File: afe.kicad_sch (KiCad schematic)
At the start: 142 parts, among them J1 Conn_01x18, Q1 Q_NMOS_GDS, Q10 Q_NMOS_GDS, Q11 Q_NMOS_GDS, Q12 Q_NMOS_GDS, Q13 Q_NMOS_GDS, Q14 Q_NMOS_GDS, Q15 Q_NMOS_GDS, Q16 Q_NMOS_GDS, Q17 Q_NMOS_GDS, Q18 Q_NMOS_GDS, Q19 Q_NMOS_GDS, Q2 Q_NMOS_GDS, Q20 Q_NMOS_GDS, Q21 Q_NMOS_GDS, Q22 Q_NMOS_GDS, Q23 Q_NMOS_GDS, Q24 Q_NMOS_GDS, Q25 Q_NMOS_GDS, Q26 Q_NMOS_GDS, Q3 Q_PMOS_GDS, Q4 Q_NPN_BCE, U1 PB7170P48

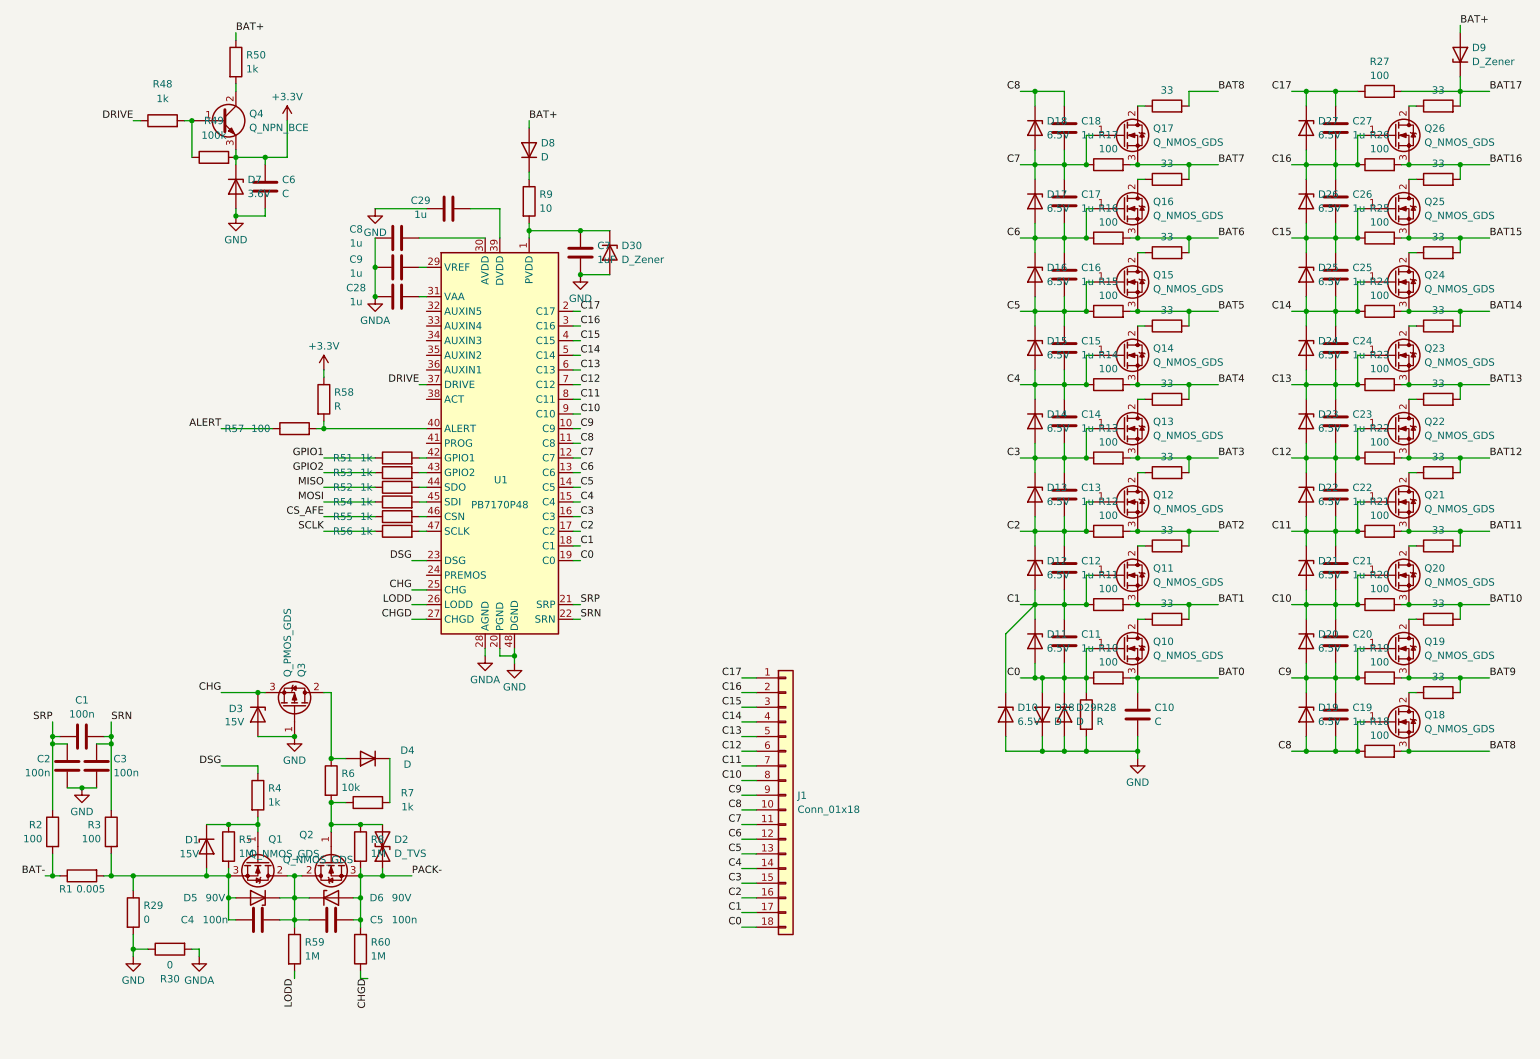
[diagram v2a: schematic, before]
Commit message: AFE改为PB7170(LQFP-64)，修改原理图，调整元器件布局
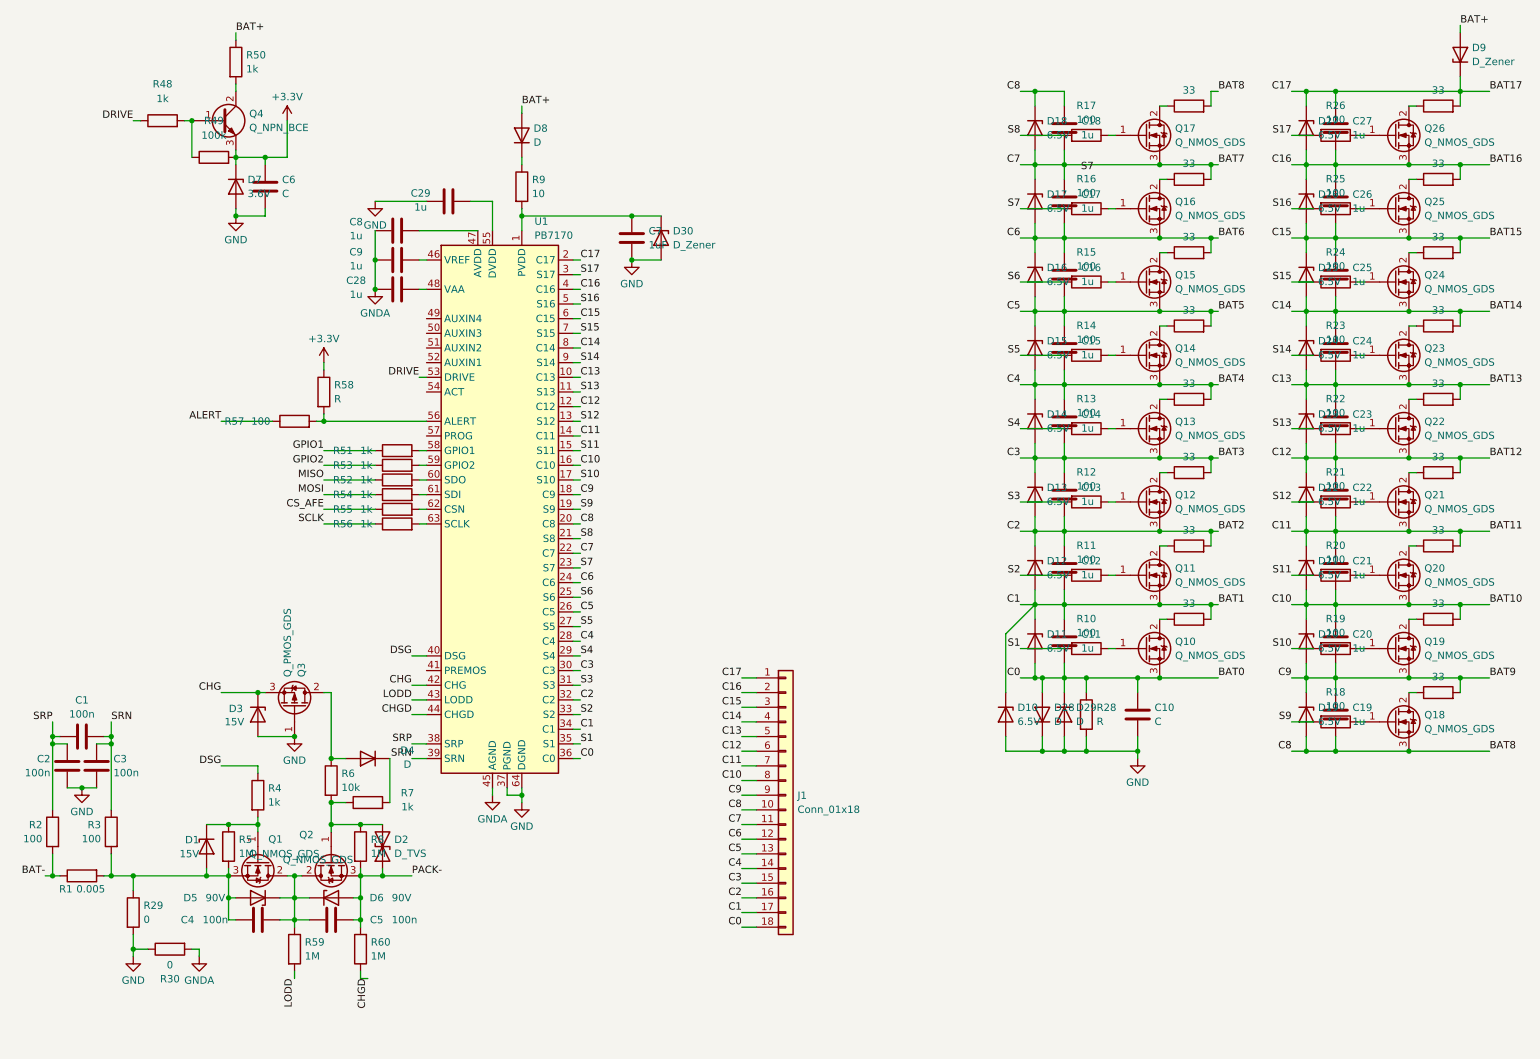
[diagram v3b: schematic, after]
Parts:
- removed R27: 100, Resistor_SMD:R_0603_1608Metric, symbol Device:R
- removed U1: PB7170P48, Package_QFP:LQFP-48_7x7mm_P0.5mm, symbol project_symbols:PB7170P48
- added U1: PB7170, Package_QFP:LQFP-64_10x10mm_P0.5mm, symbol project_symbols:PB7170
- C28, C29, C8, C9: footprint Capacitor_SMD:C_0603_1608Metric -> Capacitor_SMD:C_0402_1005Metric
- R10, R11, R12, R13, R14, R15, R16, R17, R18, R19, R2, R20, R21, R22, R23, R24, R25, R26, R3: footprint Resistor_SMD:R_0603_1608Metric -> Resistor_SMD:R_0402_1005Metric
- R31, R32, R33, R34, R35, R36, R37, R38, R39, R40, R41, R42, R43, R44, R45, R46, R47: footprint Resistor_SMD:R_0603_1608Metric -> Resistor_SMD:R_1206_3216Metric
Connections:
- net C17 is gone; now on net BAT17: C27.1, D27.1 (K), J1.1 (Pin_1)
- net BAT0: now also C11.2, D11.2 (A), D28.2 (A), D29.1 (K), J1.18 (Pin_18), R28.1, U1.36 (C0); no longer R10.2
- net BAT1: now also C11.1, C12.2, D10.1 (K), D11.1 (K), D12.2 (A), J1.17 (Pin_17), U1.34 (C1); no longer R11.2
- net BAT10: now also C20.1, C21.2, D20.1 (K), D21.2 (A), J1.8 (Pin_8), U1.16 (C10); no longer R20.2
- net BAT11: now also C21.1, C22.2, D21.1 (K), D22.2 (A), J1.7 (Pin_7), U1.14 (C11); no longer R21.2
- net BAT12: now also C22.1, C23.2, D22.1 (K), D23.2 (A), J1.6 (Pin_6), U1.12 (C12); no longer R22.2
- net BAT13: now also C23.1, C24.2, D23.1 (K), D24.2 (A), J1.5 (Pin_5), U1.10 (C13); no longer R23.2
- net BAT14: now also C24.1, C25.2, D24.1 (K), D25.2 (A), J1.4 (Pin_4), U1.8 (C14); no longer R24.2
- net BAT15: now also C25.1, C26.2, D25.1 (K), D26.2 (A), J1.3 (Pin_3), U1.6 (C15); no longer R25.2
- net BAT16: now also C26.1, C27.2, D26.1 (K), D27.2 (A), J1.2 (Pin_2), U1.4 (C16); no longer R26.2
- net BAT17: now also U1.2 (C17)
- net BAT2: now also C12.1, C13.2, D12.1 (K), D13.2 (A), J1.16 (Pin_16), U1.32 (C2); no longer R12.2
- net BAT3: now also C13.1, C14.2, D13.1 (K), D14.2 (A), J1.15 (Pin_15), U1.30 (C3); no longer R13.2
- net BAT4: now also C14.1, C15.2, D14.1 (K), D15.2 (A), J1.14 (Pin_14), U1.28 (C4); no longer R14.2
- net BAT5: now also C15.1, C16.2, D15.1 (K), D16.2 (A), J1.13 (Pin_13), U1.26 (C5); no longer R15.2
- net BAT6: now also C16.1, C17.2, D16.1 (K), D17.2 (A), J1.12 (Pin_12), U1.24 (C6); no longer R16.2
- net BAT7: now also C17.1, C18.2, D17.1 (K), D18.2 (A), J1.11 (Pin_11), U1.22 (C7); no longer R17.2
- net BAT8: now also C18.1, C19.2, D18.1 (K), D19.2 (A), J1.10 (Pin_10), U1.20 (C8); no longer R18.2
- net BAT9: now also C19.1, C20.2, D19.1 (K), D20.2 (A), J1.9 (Pin_9), U1.18 (C9); no longer R19.2
- net CHG: now also U1.42 (CHG)
- net CHGD: now also U1.44 (CHGD)
- net DRIVE: now also U1.53 (DRIVE)
- net DSG: now also U1.40 (DSG)
- net GND: now also U1.37 (PGND), U1.64 (DGND)
- net GNDA: now also U1.45 (AGND)
- net LODD: now also U1.43 (LODD)
- net SRN: now also U1.39 (SRN)
- net SRP: now also U1.38 (SRP)
- net at R54.2: now also U1.61 (SDI)
- net at C7.1, D30.1 (K), R9.2: now also U1.1 (PVDD)
- net at R53.2: now also U1.59 (GPIO2)
- net at C28.2: now also U1.48 (VAA)
- net at R52.2: now also U1.60 (SDO)
- net at C29.2: now also U1.55 (DVDD)
- net at R56.2: now also U1.63 (SCLK)
- net at C9.2: now also U1.46 (VREF)
- net at C8.2: now also U1.47 (AVDD)
- net at R57.2, R58.2: now also U1.56 (ALERT)
- net at R51.2: now also U1.58 (GPIO1)
- net at R55.2: now also U1.62 (CSN)
- removed net C0: C11.2, D11.2 (A), D28.2 (A), D29.1 (K), J1.18 (Pin_18), Q10.1 (G), R10.1, R28.1
- removed net C1: C11.1, C12.2, D10.1 (K), D11.1 (K), D12.2 (A), J1.17 (Pin_17), Q11.1 (G), R11.1
- removed net C10: C20.1, C21.2, D20.1 (K), D21.2 (A), J1.8 (Pin_8), Q20.1 (G), R20.1
- removed net C11: C21.1, C22.2, D21.1 (K), D22.2 (A), J1.7 (Pin_7), Q21.1 (G), R21.1
- removed net C12: C22.1, C23.2, D22.1 (K), D23.2 (A), J1.6 (Pin_6), Q22.1 (G), R22.1
- removed net C13: C23.1, C24.2, D23.1 (K), D24.2 (A), J1.5 (Pin_5), Q23.1 (G), R23.1
- removed net C14: C24.1, C25.2, D24.1 (K), D25.2 (A), J1.4 (Pin_4), Q24.1 (G), R24.1
- removed net C15: C25.1, C26.2, D25.1 (K), D26.2 (A), J1.3 (Pin_3), Q25.1 (G), R25.1
- removed net C16: C26.1, C27.2, D26.1 (K), D27.2 (A), J1.2 (Pin_2), Q26.1 (G), R26.1
- removed net C2: C12.1, C13.2, D12.1 (K), D13.2 (A), J1.16 (Pin_16), Q12.1 (G), R12.1
- removed net C3: C13.1, C14.2, D13.1 (K), D14.2 (A), J1.15 (Pin_15), Q13.1 (G), R13.1
- removed net C4: C14.1, C15.2, D14.1 (K), D15.2 (A), J1.14 (Pin_14), Q14.1 (G), R14.1
- removed net C5: C15.1, C16.2, D15.1 (K), D16.2 (A), J1.13 (Pin_13), Q15.1 (G), R15.1
- removed net C6: C16.1, C17.2, D16.1 (K), D17.2 (A), J1.12 (Pin_12), Q16.1 (G), R16.1
- removed net C7: C17.1, C18.2, D17.1 (K), D18.2 (A), J1.11 (Pin_11), Q17.1 (G), R17.1
- removed net C8: C18.1, C19.2, D18.1 (K), D19.2 (A), J1.10 (Pin_10), Q18.1 (G), R18.1
- removed net C9: C19.1, C20.2, D19.1 (K), D20.2 (A), J1.9 (Pin_9), Q19.1 (G), R19.1
- new net: Q18.1 (G), R18.1
- new net: Q19.1 (G), R19.1
- new net: Q13.1 (G), R13.1
- new net: Q20.1 (G), R20.1
- new net: Q12.1 (G), R12.1
- new net: Q22.1 (G), R22.1
- new net: Q10.1 (G), R10.1
- new net: Q16.1 (G), R16.1
- new net: Q25.1 (G), R25.1
- new net: Q17.1 (G), R17.1
- new net: Q23.1 (G), R23.1
- new net: Q26.1 (G), R26.1
- new net: Q24.1 (G), R24.1
- new net: Q21.1 (G), R21.1
- new net: Q14.1 (G), R14.1
- new net: Q11.1 (G), R11.1
- new net: Q15.1 (G), R15.1
- new net S1: R10.2, U1.35 (S1)
- new net S10: R19.2, U1.17 (S10)
- new net S11: R20.2, U1.15 (S11)
- new net S12: R21.2, U1.13 (S12)
- new net S13: R22.2, U1.11 (S13)
- new net S14: R23.2, U1.9 (S14)
- new net S15: R24.2, U1.7 (S15)
- new net S16: R25.2, U1.5 (S16)
- new net S17: R26.2, U1.3 (S17)
- new net S2: R11.2, U1.33 (S2)
- new net S3: R12.2, U1.31 (S3)
- new net S4: R13.2, U1.29 (S4)
- new net S5: R14.2, U1.27 (S5)
- new net S6: R15.2, U1.25 (S6)
- new net S7: R16.2, U1.23 (S7)
- new net S8: R17.2, U1.21 (S8)
- new net S9: R18.2, U1.19 (S9)
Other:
- moved on the sheet: C28, C29, C7, C8, C9, D30, D8, Q10, Q11, Q12, Q13, Q14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

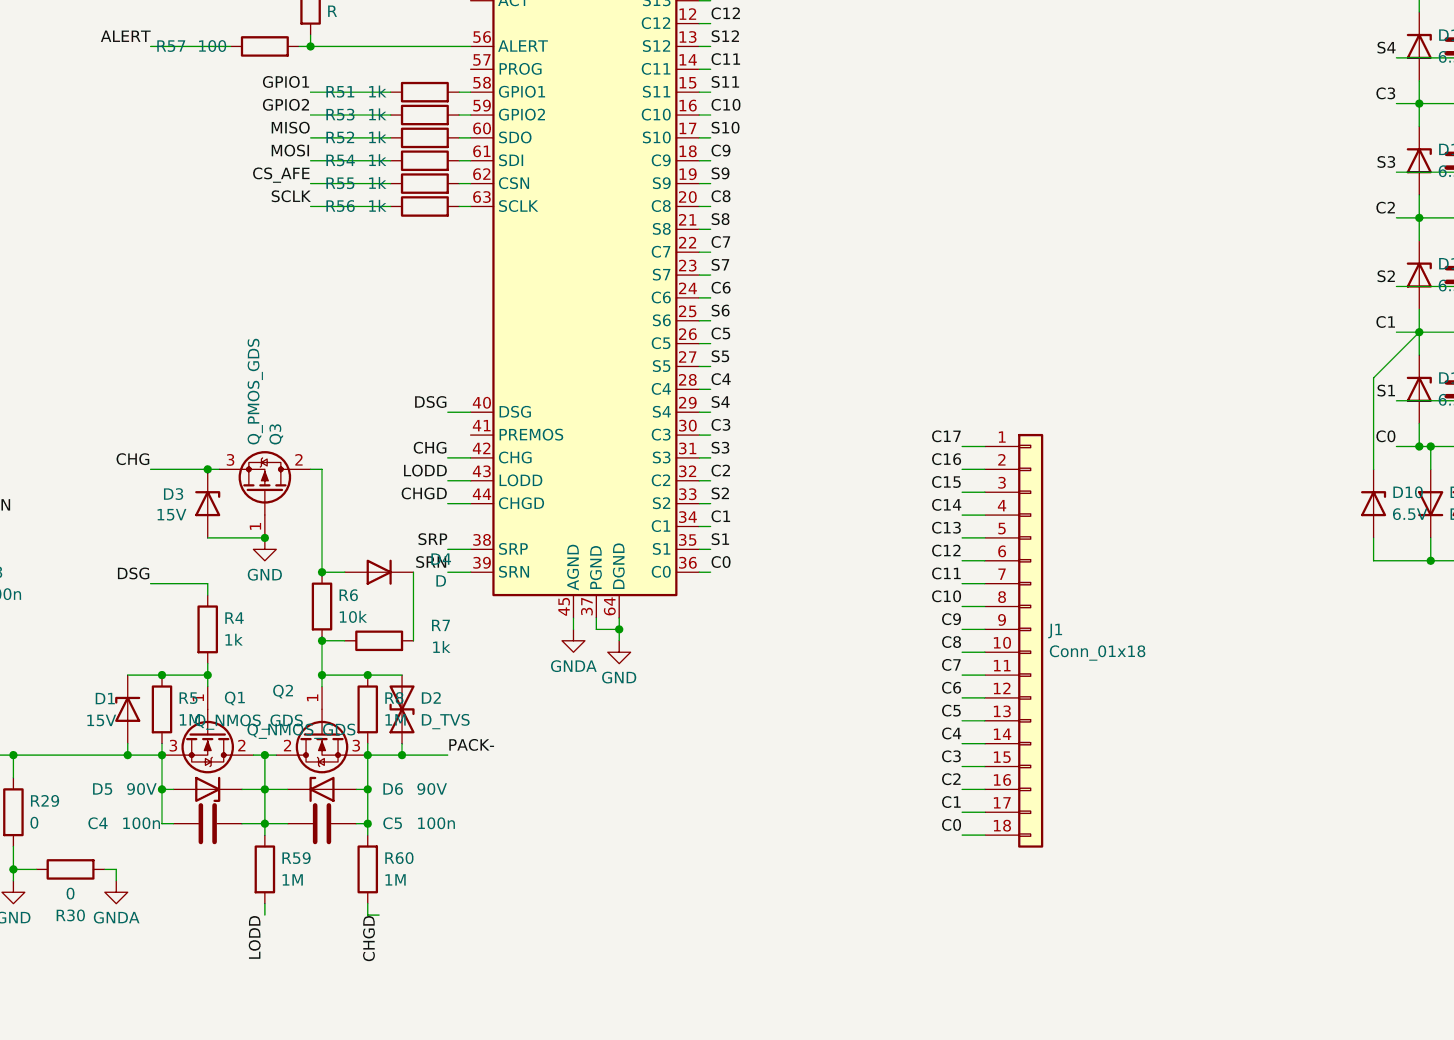
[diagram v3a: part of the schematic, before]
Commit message: 充放电MOS管改为6个并联
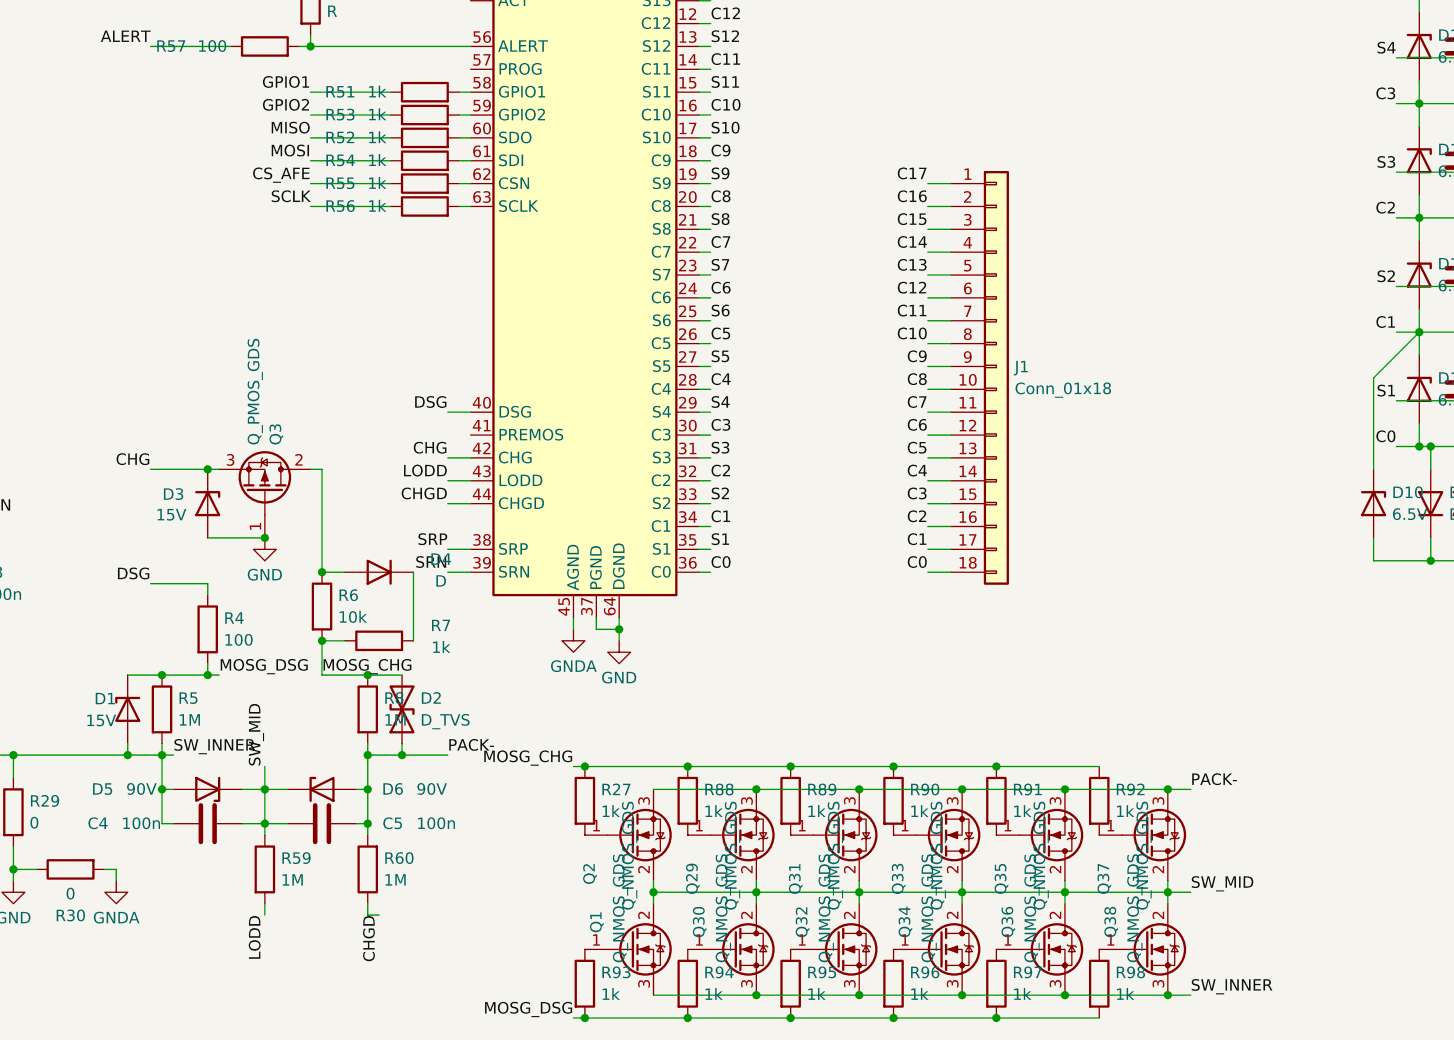
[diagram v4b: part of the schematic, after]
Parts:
- added Q29, Q30, Q31, Q32, Q33, Q34, Q35, Q36, Q37, Q38: Q_NMOS_GDS, Package_TO_SOT_SMD:TO-252-2, symbol Device:Q_NMOS_GDS
- added R27, R88, R89, R90, R91, R92, R93, R94, R95, R96, R97, R98: 1k, Resistor_SMD:R_0603_1608Metric, symbol Device:R
- R4: value 1k -> 100; footprint Resistor_SMD:R_0402_1005Metric -> Resistor_SMD:R_0603_1608Metric
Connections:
- net PACK-: now also Q29.3 (S), Q31.3 (S), Q33.3 (S), Q35.3 (S), Q37.3 (S)
- net SW_INNER: now reaches C4.1, D1.2 (A), D5.2 (A), Q1.3 (S), R1.2, R29.1, R3.2, R5.2
- net SW_INNER: now also Q30.3 (S), Q32.3 (S), Q34.3 (S), Q36.3 (S), Q38.3 (S)
- net MOSG_CHG: now reaches D2.2 (A2), R6.2, R7.1, R8.1
- net MOSG_CHG: now also R27.1, R88.1, R89.1, R90.1, R91.1, R92.1; no longer Q2.1 (G)
- net MOSG_DSG: now reaches D1.1 (K), R4.2, R5.1
- net MOSG_DSG: now also R93.2, R94.2, R95.2, R96.2, R97.2, R98.2; no longer Q1.1 (G)
- net SW_MID: now reaches C4.2, C5.1, D5.1 (K), D6.1 (K), Q1.2 (D), Q2.2 (D), R59.1
- net SW_MID: now also Q29.2 (D), Q30.2 (D), Q31.2 (D), Q32.2 (D), Q33.2 (D), Q34.2 (D), Q35.2 (D), Q36.2 (D), Q37.2 (D), Q38.2 (D)
- new net: Q31.1 (G), R89.2
- new net: Q33.1 (G), R90.2
- new net: Q32.1 (G), R95.1
- new net: Q37.1 (G), R92.2
- new net: Q36.1 (G), R97.1
- new net: Q38.1 (G), R98.1
- new net: Q35.1 (G), R91.2
- new net: Q34.1 (G), R96.1
- new net: Q30.1 (G), R94.1
- new net: Q2.1 (G), R27.2
- new net: Q29.1 (G), R88.2
- new net: Q1.1 (G), R93.1
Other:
- moved on the sheet: J1, Q1, Q2

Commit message: 分配封装和在PCB上大致布局
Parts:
- Q4: value Q_NPN_BCE -> Q_NPN_BEC; symbol Device:Q_NPN_BCE -> Device:Q_NPN_BEC
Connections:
- net +3.3V: now also Q4.2 (E); no longer Q4.3 (E)
- net at R50.2: now also Q4.3 (C); no longer Q4.2 (C)
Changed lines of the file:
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@@
 	)
 	(symbol
-		(lib_id "Device:Q_NPN_BCE")
+		(lib_id "Device:Q_NPN_BEC")
 		(at 53.34 35.56 0)
 		(unit 1)
@@
 			)
 		)
-		(property "Value" "Q_NPN_BCE"
-			(at 58.1914 36.7721 0)
+		(property "Value" "Q_NPN_BEC"
+			(at 58.42 36.83 0)
 			(effects
 				(font
@@
 			)
 		)
-		(property "Description" "NPN transistor, base/collector/emitter"
+		(property "Description" "NPN transistor, base/emitter/collector"
 			(at 53.34 35.56 0)
 			(effects
